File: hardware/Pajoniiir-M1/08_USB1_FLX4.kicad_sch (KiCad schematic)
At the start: 9 parts

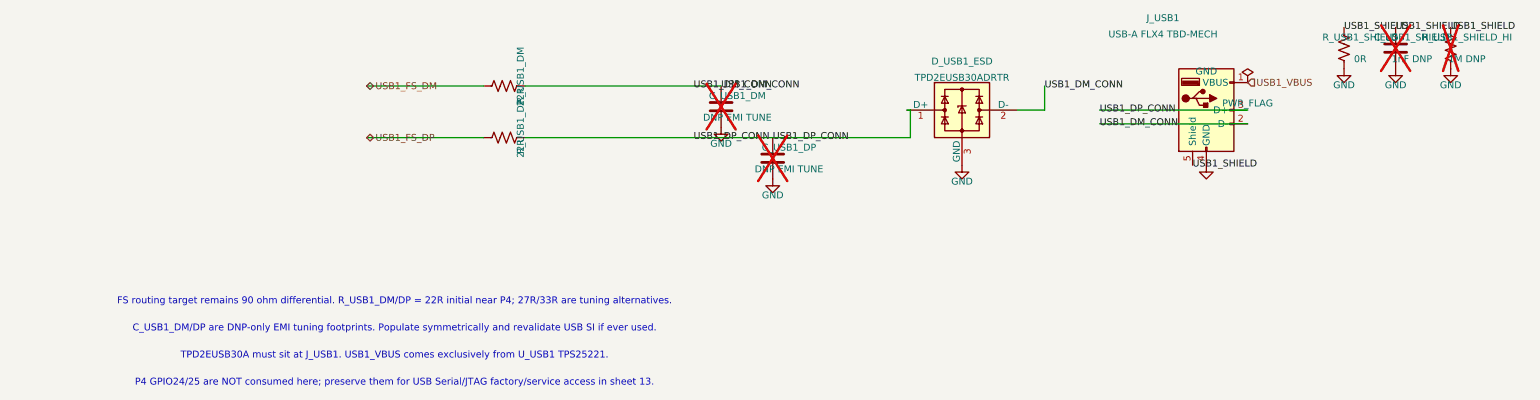
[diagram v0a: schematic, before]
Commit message: hardware: normalize schematic reference designators
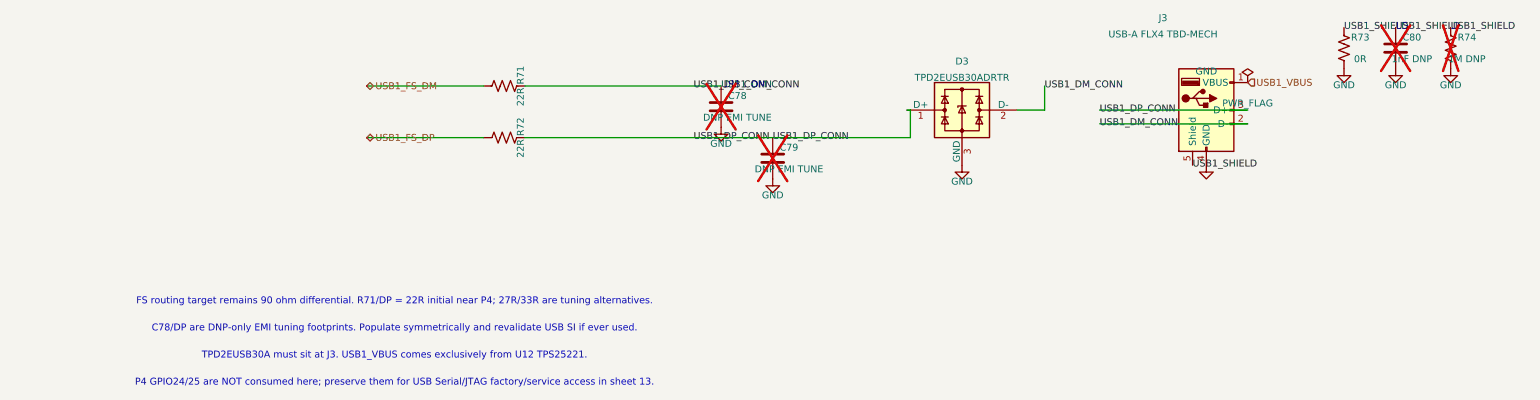
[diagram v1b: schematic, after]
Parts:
- renumbered C_USB1_DM to C78, C_USB1_DP to C79, C_USB1_SHIELD to C80, D_USB1_ESD to D3, J_USB1 to J3, R_USB1_DM to R71, R_USB1_DP to R72, R_USB1_SHIELD to R73, R_USB1_SHIELD_HI to R74
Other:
- note added: "C78/DP are DNP-only EMI tuning footprints. Populate symmetrically and revalidate USB SI if ever used."
- note added: "FS routing target remains 90 ohm differential. R71/DP = 22R initial near P4; 27R/33R are tuning alternatives."
- note added: "TPD2EUSB30A must sit at J3. USB1_VBUS comes exclusively from U12 TPS25221."
- note removed: "C_USB1_DM/DP are DNP-only EMI tuning footprints. Populate symmetrically and revalidate USB SI if ever used."
- note removed: "FS routing target remains 90 ohm differential. R_USB1_DM/DP = 22R initial near P4; 27R/33R are tuning alternatives."
- note removed: "TPD2EUSB30A must sit at J_USB1. USB1_VBUS comes exclusively from U_USB1 TPS25221."

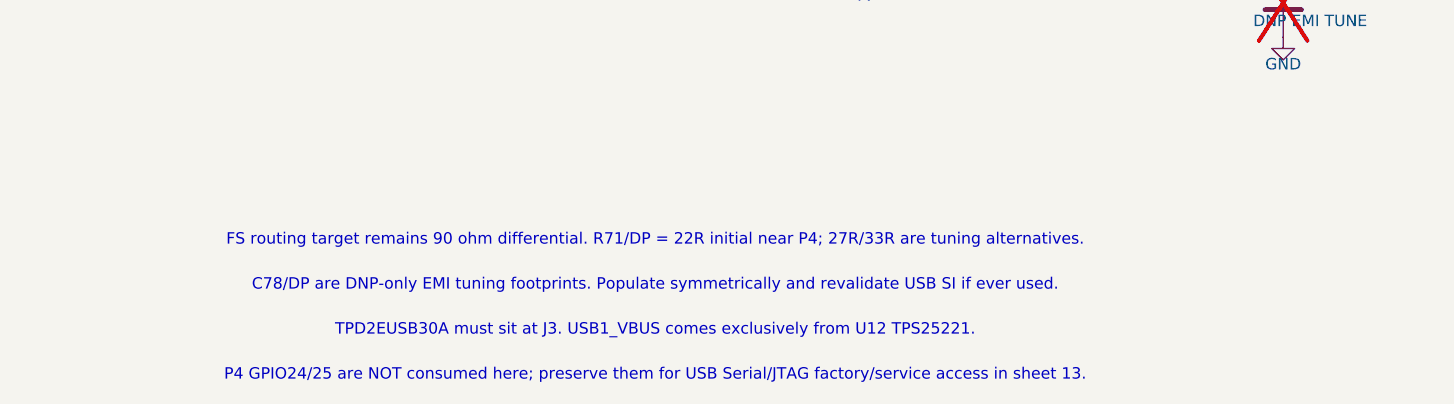
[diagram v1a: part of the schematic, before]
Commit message: hardware: constrain RefDes migration to annotation fields
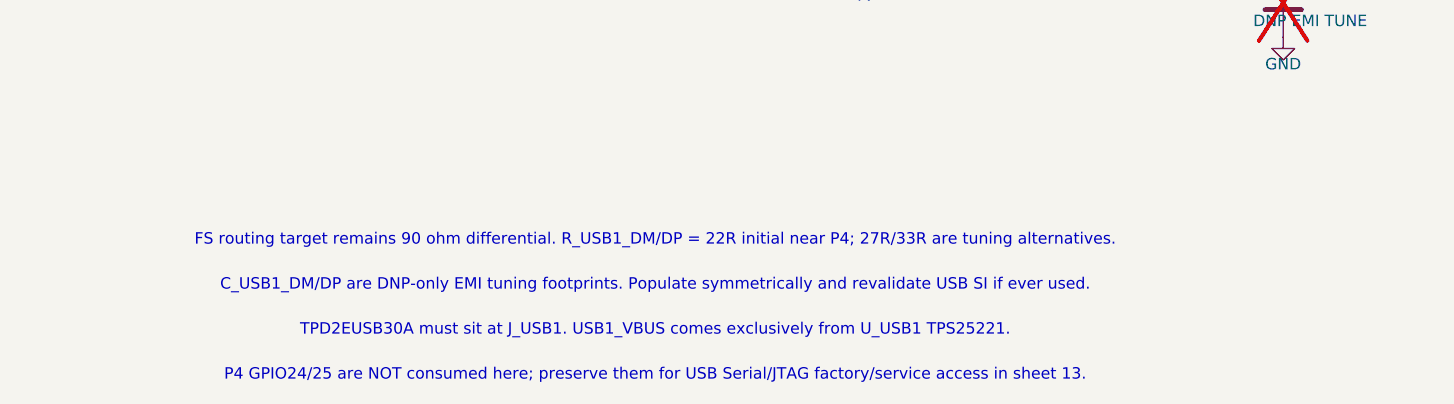
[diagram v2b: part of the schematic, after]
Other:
- note added: "C_USB1_DM/DP are DNP-only EMI tuning footprints. Populate symmetrically and revalidate USB SI if ever used."
- note added: "FS routing target remains 90 ohm differential. R_USB1_DM/DP = 22R initial near P4; 27R/33R are tuning alternatives."
- note added: "TPD2EUSB30A must sit at J_USB1. USB1_VBUS comes exclusively from U_USB1 TPS25221."
- note removed: "C78/DP are DNP-only EMI tuning footprints. Populate symmetrically and revalidate USB SI if ever used."
- note removed: "FS routing target remains 90 ohm differential. R71/DP = 22R initial near P4; 27R/33R are tuning alternatives."
- note removed: "TPD2EUSB30A must sit at J3. USB1_VBUS comes exclusively from U12 TPS25221."
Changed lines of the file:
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@@
     (instances (project "Pajoniiir-M1" (path "/2c8dd352-b7b8-4d9e-8f93-5dd43be2a100/31000008-6b2a-4a3a-8c91-000000000008" (reference "#PWR0807") (unit 1))))
   )
-  (text "FS routing target remains 90 ohm differential. R71/DP = 22R initial near P4; 27R/33R are tuning alternatives." (exclude_from_sim no) (at 35 95 0) (effects (font (size 1.27 1.27))))
-  (text "C78/DP are DNP-only EMI tuning footprints. Populate symmetrically and revalidate USB SI if ever used." (exclude_from_sim no) (at 35 100 0) (effects (font (size 1.27 1.27))))
-  (text "TPD2EUSB30A must sit at J3. USB1_VBUS comes exclusively from U12 TPS25221." (exclude_from_sim no) (at 35 105 0) (effects (font (size 1.27 1.27))))
+  (text "FS routing target remains 90 ohm differential. R_USB1_DM/DP = 22R initial near P4; 27R/33R are tuning alternatives." (exclude_from_sim no) (at 35 95 0) (effects (font (size 1.27 1.27))))
+  (text "C_USB1_DM/DP are DNP-only EMI tuning footprints. Populate symmetrically and revalidate USB SI if ever used." (exclude_from_sim no) (at 35 100 0) (effects (font (size 1.27 1.27))))
+  (text "TPD2EUSB30A must sit at J_USB1. USB1_VBUS comes exclusively from U_USB1 TPS25221." (exclude_from_sim no) (at 35 105 0) (effects (font (size 1.27 1.27))))
   (text "P4 GPIO24/25 are NOT consumed here; preserve them for USB Serial/JTAG factory/service access in sheet 13." (exclude_from_sim no) (at 35 110 0) (effects (font (size 1.27 1.27))))
   (symbol
